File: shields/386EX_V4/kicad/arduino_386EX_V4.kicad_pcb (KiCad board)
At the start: 4 copper layers, 93.3 x 60.3 mm, 50 parts, among them J1 Conn_01x02_Pin, J2 JTAG, J3 Conn_01x04_Pin, J4 Conn_01x04_Pin, J5 Conn_01x04_Pin, J6 SERIAL0, J9 WP Jumper, U1 AT24CS01-STUM, U11 I386EX_PQFP, U2 ULN2003A, U3 SN74LV14A

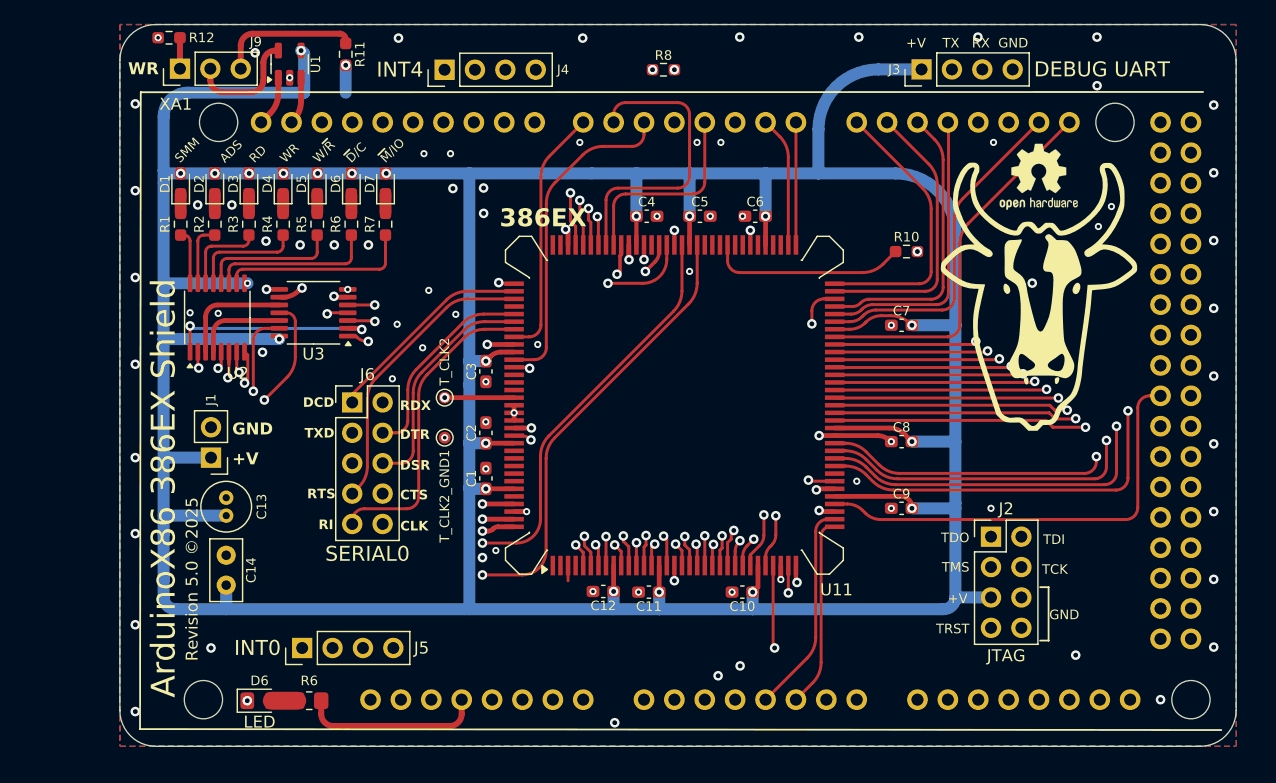
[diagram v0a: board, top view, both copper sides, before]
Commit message: Added I2C SDA, SCK, ~ERROR and ~LOCK pull-up resistors; resolved minor DRC errors.
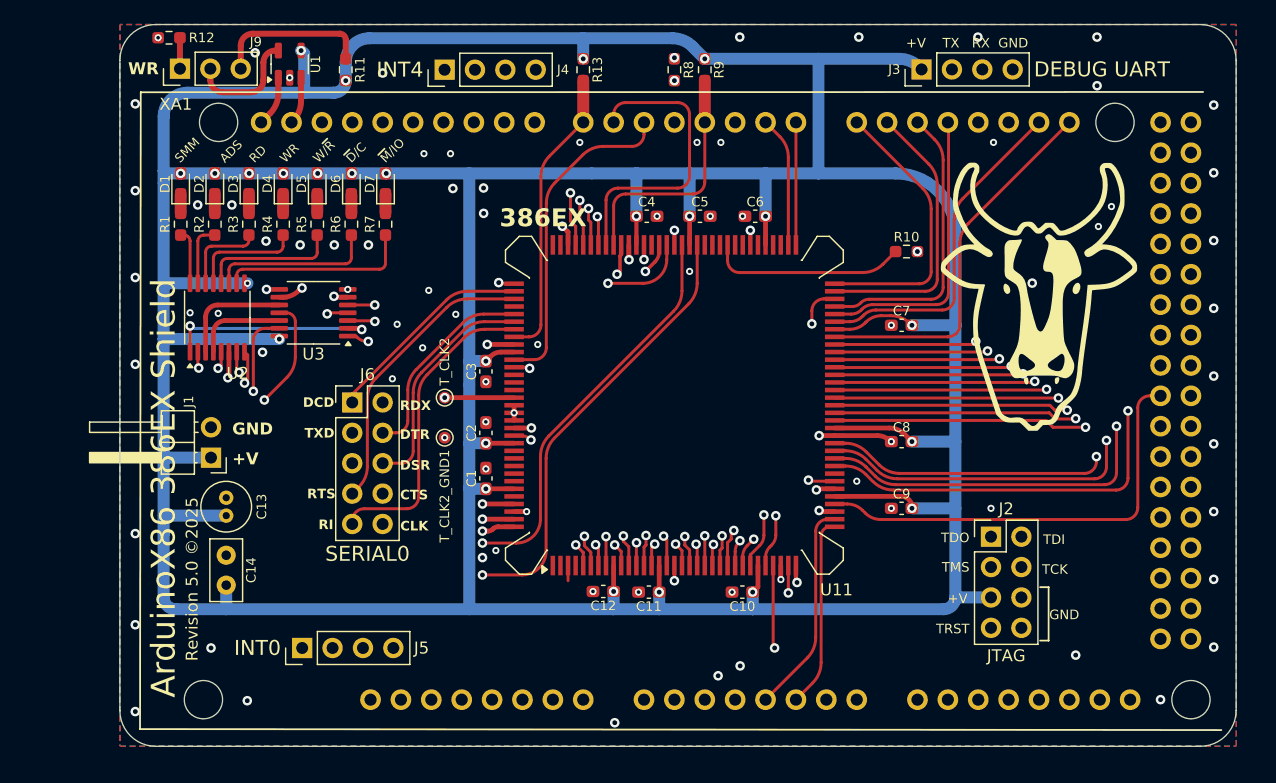
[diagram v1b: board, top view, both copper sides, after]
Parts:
- removed the D6 at (122.2, 120.7)
- removed the R6 at (126.3, 120.7)
- removed REF**: OSHW-Logo2_7.3x6mm_SilkScreen, Symbol:OSHW-Logo2_7.3x6mm_SilkScreen
- added R13: 3.3 K Ohm, Resistor_SMD:R_0603_1608Metric_Pad0.98x0.95mm_HandSolder, F.Cu at (149.2, 67.9)
- added R9: 3.3 K Ohm, Resistor_SMD:R_0603_1608Metric_Pad0.98x0.95mm_HandSolder, F.Cu at (159.4, 67.9)
- C1, C10, C11, C12, C2, C3, C4, C5, C6, C7, C8, C9: value C -> 0.1 uF
- J1: footprint Connector_PinHeader_2.54mm:PinHeader_1x02_P2.54mm_Vertical -> Connector_PinHeader_2.54mm:PinHeader_1x02_P2.54mm_Horizontal
- R11, R12: value R -> 3.3 K Ohm
- moved R11 1.29 mm to (129.4, 67.9)
- moved R8 0.91 mm to (156.8, 67.9), turned to 90 degrees
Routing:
- net +3.3VP: track 380.8 -> 430.4 mm, vias 23 -> 25
- net +3.3V: track 15.1 -> 0.00 mm
- net ~{LOCK}: track 21.1 -> 24.5 mm
- net ~{ERROR}: track 16.9 -> 20.4 mm
- net Net-(U11-CLK2): track 44.0 -> 46.1 mm
- net Net-(D6-A): track 2.13 -> 0.00 mm
- net Net-(J9-Pin_3): track 11.8 -> 13.1 mm
- net /ADS: track 18.1 -> 17.1 mm
- net CLOCK: track 4.40 -> 3.49 mm
- net GND: track 24.0 -> 24.4 mm, vias 86 -> 85

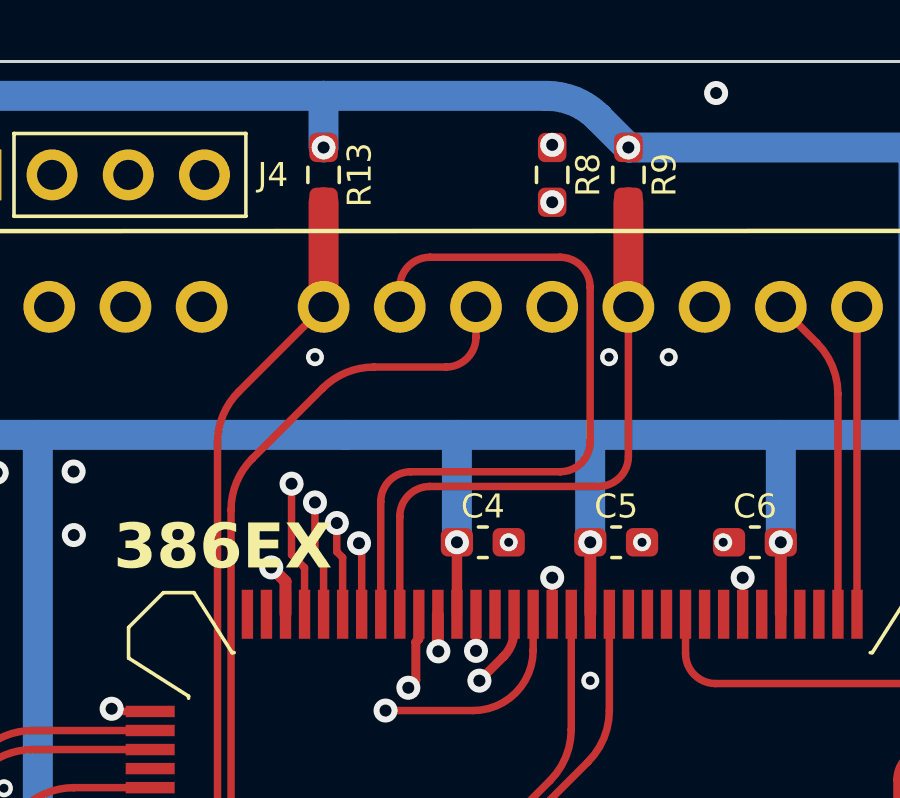
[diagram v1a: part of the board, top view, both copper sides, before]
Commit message: Fixed bug from previous commit, R13 was wired to ~LOCK, was supposed to be to ~BUSY, corrected in this commit.
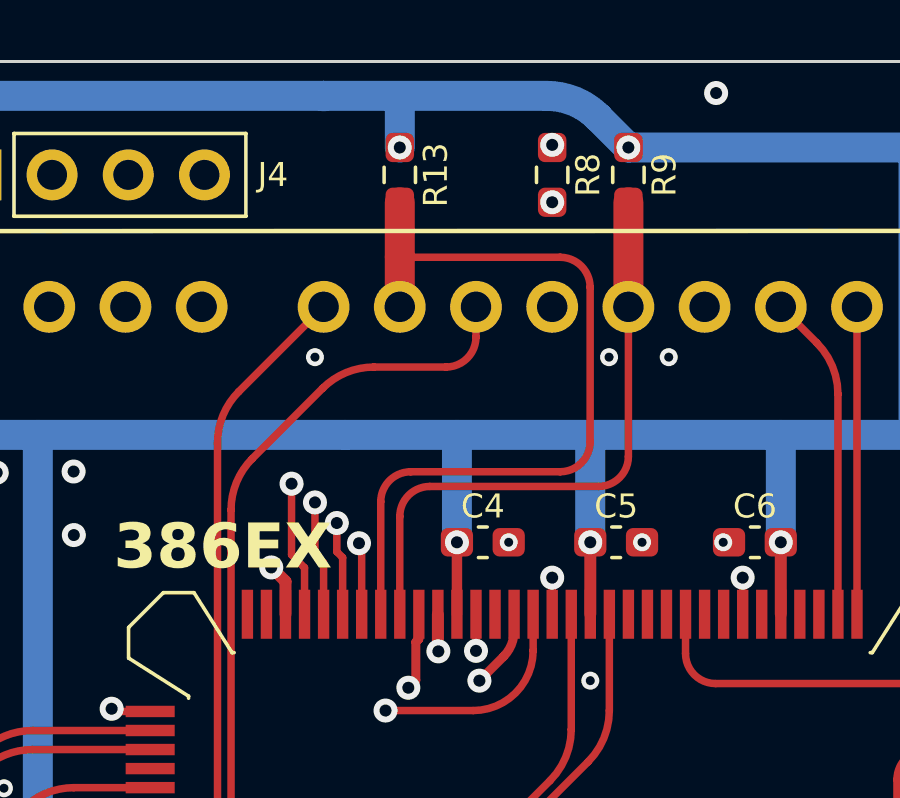
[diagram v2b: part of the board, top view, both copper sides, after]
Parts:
- moved R13 2.54 mm to (151.8, 67.9)
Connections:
- R13 pad 1: ~{LOCK} -> ~{BUSY}
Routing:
- net ~{LOCK}: track 24.5 -> 21.1 mm
- net ~{BUSY}: track 25.0 -> 27.3 mm
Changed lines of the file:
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@@
 	(footprint "Resistor_SMD:R_0603_1608Metric_Pad0.98x0.95mm_HandSolder"
 		(layer "F.Cu")
-		(at 149.225 67.903872 90)
+		(at 151.765 67.903872 90)
 		(descr "Resistor SMD 0603 (1608 Metric), square (rectangular) end terminal, IPC-7351 nominal with elongated pad for handsoldering. (Body size source: IPC-SM-782 page 72, https://www.pcb-3d.com/wordpress/wp-content/uploads/ipc-sm-782a_amendment_1_and_2.pdf), generated with kicad-footprint-generator")
 		(tags "resistor handsolder")
@@
 			(layers "F.Cu" "F.Mask" "F.Paste")
 			(roundrect_rratio 0.25)
-			(net 101 "~{LOCK}")
+			(net 99 "~{BUSY}")
 			(pintype "passive")
 		)
@@
 	)
 	(via
-		(at 149.225 66.991372)
+		(at 151.765 66.991372)
 		(size 0.8)
 		(drill 0.4)
@@
 	)
 	(segment
-		(start 149.225 66.991372)
-		(end 149.225 65.285)
+		(start 151.765 66.991372)
+		(end 151.765 65.285)
 		(width 1)
 		(layer "B.Cu")
@@
 	)
 	(segment
-		(start 157.11 70.65)
-		(end 152.765 70.65)
+		(start 151.13 82.55)
+		(end 151.13 78.8)
 		(width 0.25)
 		(layer "F.Cu")
@@
 	)
 	(segment
-		(start 158.11 71.65)
-		(end 158.11 76.8)
+		(start 157.11 70.65)
+		(end 151.775 70.65)
 		(width 0.25)
 		(layer "F.Cu")
@@
 	)
 	(segment
-		(start 152.13 77.8)
-		(end 157.11 77.8)
-		(width 0.25)
+		(start 151.765 72.3025)
+		(end 151.765 70.64)
+		(width 1)
 		(layer "F.Cu")
 		(net 99)
 	)
 	(segment
-		(start 151.13 78.8)
-		(end 151.13 82.55)
+		(start 158.11 76.8)
+		(end 158.11 71.65)
 		(width 0.25)
 		(layer "F.Cu")
@@
 	)
 	(segment
-		(start 151.765 71.65)
-		(end 151.765 72.3025)
+		(start 151.775 70.65)
+		(end 151.765 70.64)
 		(width 0.25)
 		(layer "F.Cu")
 		(net 99)
 	)
-	(arc
-		(start 158.11 71.65)
-		(mid 157.817106 70.942893)
-		(end 157.11 70.65)
+	(segment
+		(start 151.765 70.64)
+		(end 151.765 68.816372)
+		(width 1)
+		(layer "F.Cu")
+		(net 99)
+	)
+	(segment
+		(start 152.13 77.8)
+		(end 157.11 77.8)
 		(width 0.25)
 		(layer "F.Cu")
@@
 	)
 	(arc
-		(start 152.13 77.8)
+		(start 151.13 78.8)
 		(mid 151.422893 78.092893)
-		(end 151.13 78.8)
+		(end 152.13 77.8)
 		(width 0.25)
 		(layer "F.Cu")
@@
 	)
 	(arc
-		(start 158.11 76.8)
+		(start 157.11 77.8)
 		(mid 157.817106 77.507106)
-		(end 157.11 77.8)
+		(end 158.11 76.8)
 		(width 0.25)
 		(layer "F.Cu")
@@
 	)
 	(arc
-		(start 151.765 71.65)
-		(mid 152.057893 70.942893)
-		(end 152.765 70.65)
+		(start 158.11 71.65)
+		(mid 157.817106 70.942893)
+		(end 157.11 70.65)
 		(width 0.25)
 		(layer "F.Cu")
@@
 		(layer "F.Cu")
 		(net 101)
-	)
-	(segment
-		(start 149.225 72.3025)
-		(end 149.225 68.816372)
-		(width 1)
-		(layer "F.Cu")
-		(net 101)

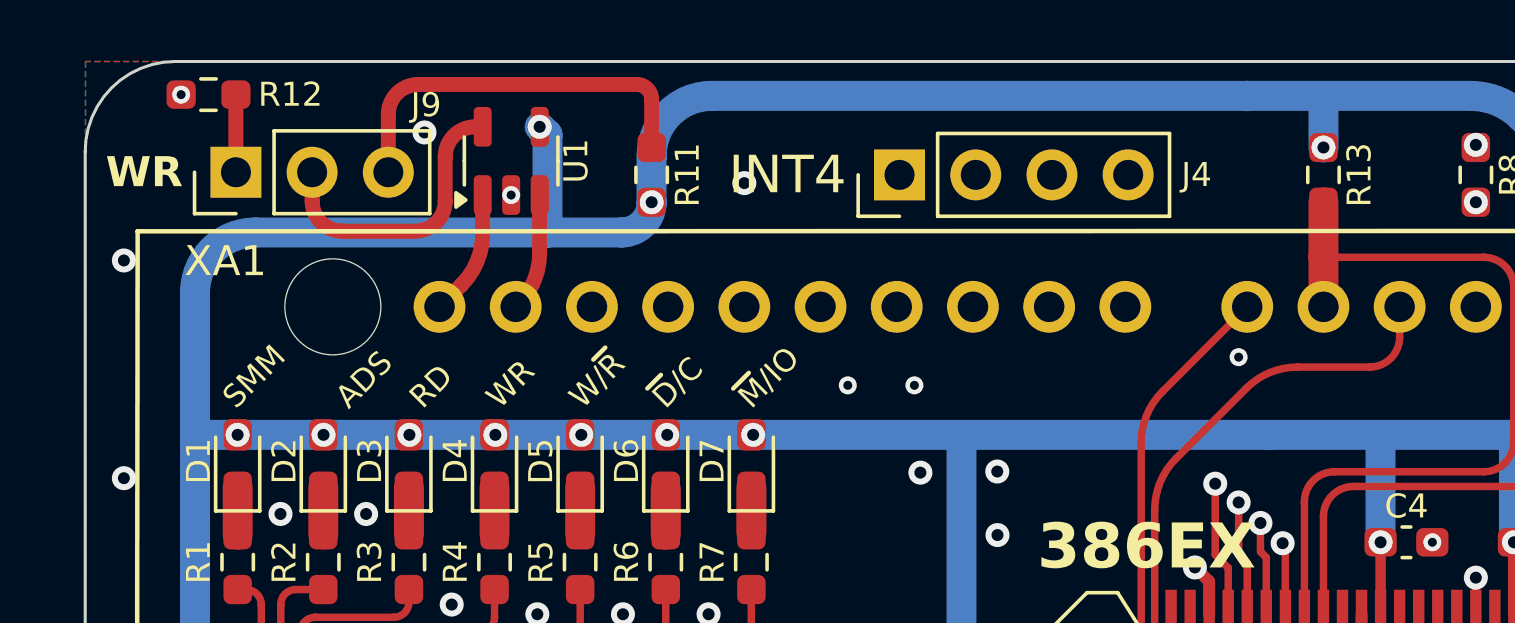
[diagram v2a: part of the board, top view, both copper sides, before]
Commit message: Fixed oversight of I2C SDA and SCK pull-up resistors; rearranged EEPROM IC to accommodate.
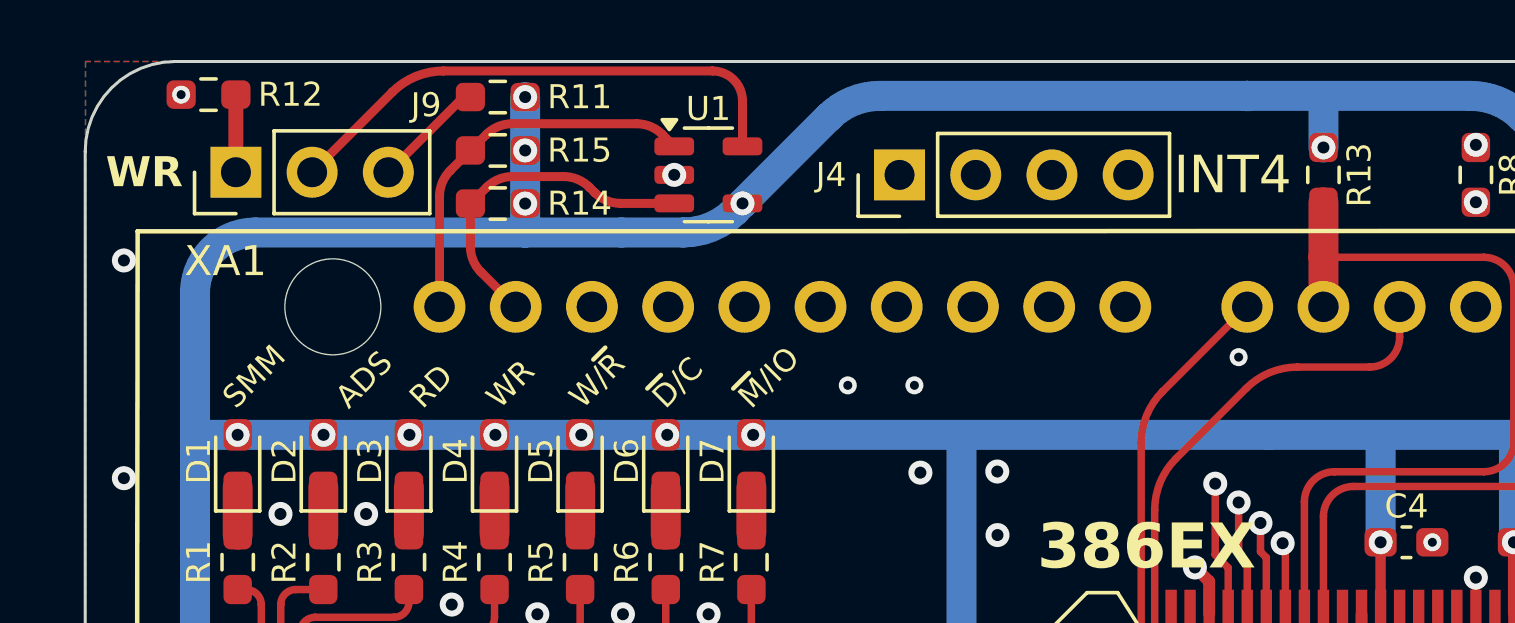
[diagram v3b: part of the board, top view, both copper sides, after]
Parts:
- added R14: 3.3 K Ohm, Resistor_SMD:R_0603_1608Metric_Pad0.98x0.95mm_HandSolder, F.Cu at (124.2, 68.9)
- added R15: 3.3 K Ohm, Resistor_SMD:R_0603_1608Metric_Pad0.98x0.95mm_HandSolder, F.Cu at (124.2, 67.1)
- moved U1 6.59 mm to (131.3, 67.9), turned to 0 degrees
- moved R11 5.75 mm to (124.2, 65.3), turned to 0 degrees
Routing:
- net Net-(J9-Pin_3): track 13.1 -> 3.77 mm
- net SCL: track 4.21 -> 12.9 mm
- net /WP: track 9.72 -> 17.7 mm
- net SDA: track 3.94 -> 11.5 mm
- net +3.3VP: track 430.4 -> 429.8 mm, vias 25 -> 27
- net GND: vias 85 -> 83

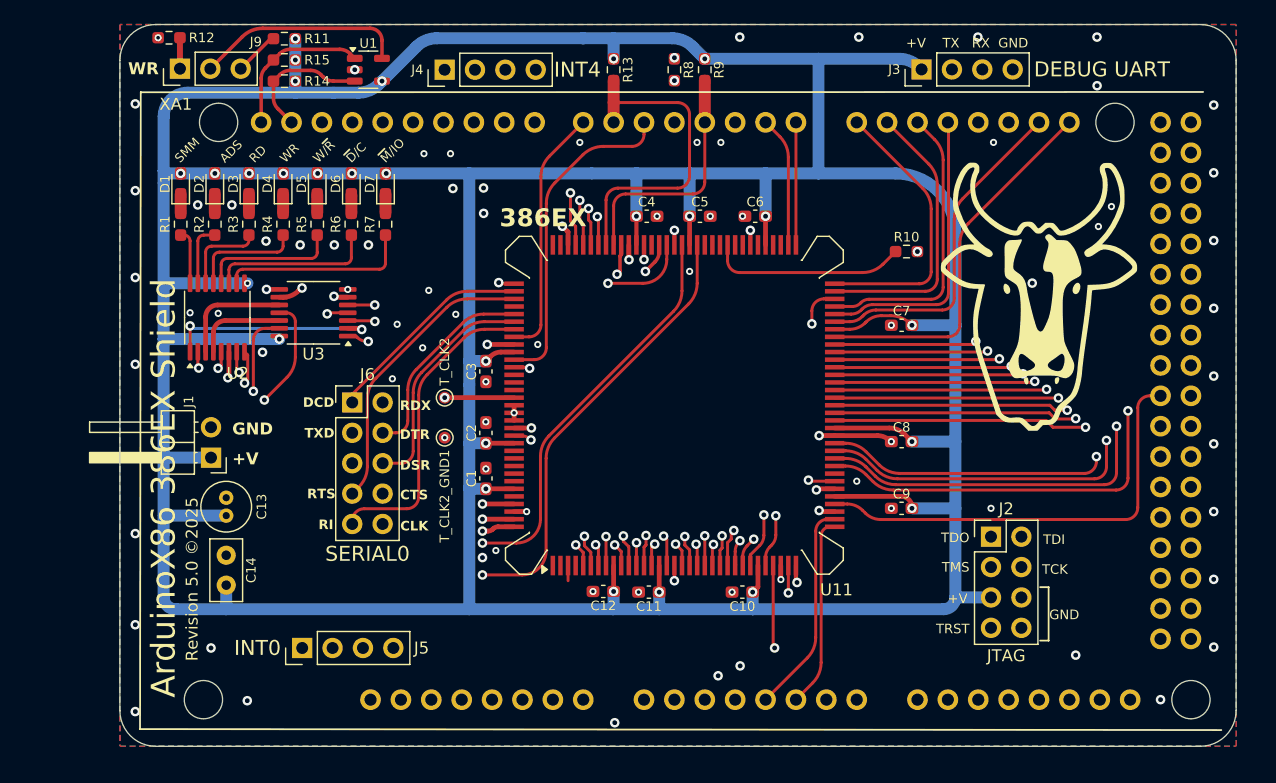
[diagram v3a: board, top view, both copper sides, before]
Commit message: Added 2x 1N4148 diodes for combining 3.3V off-board supplies, updated HTML BOM.
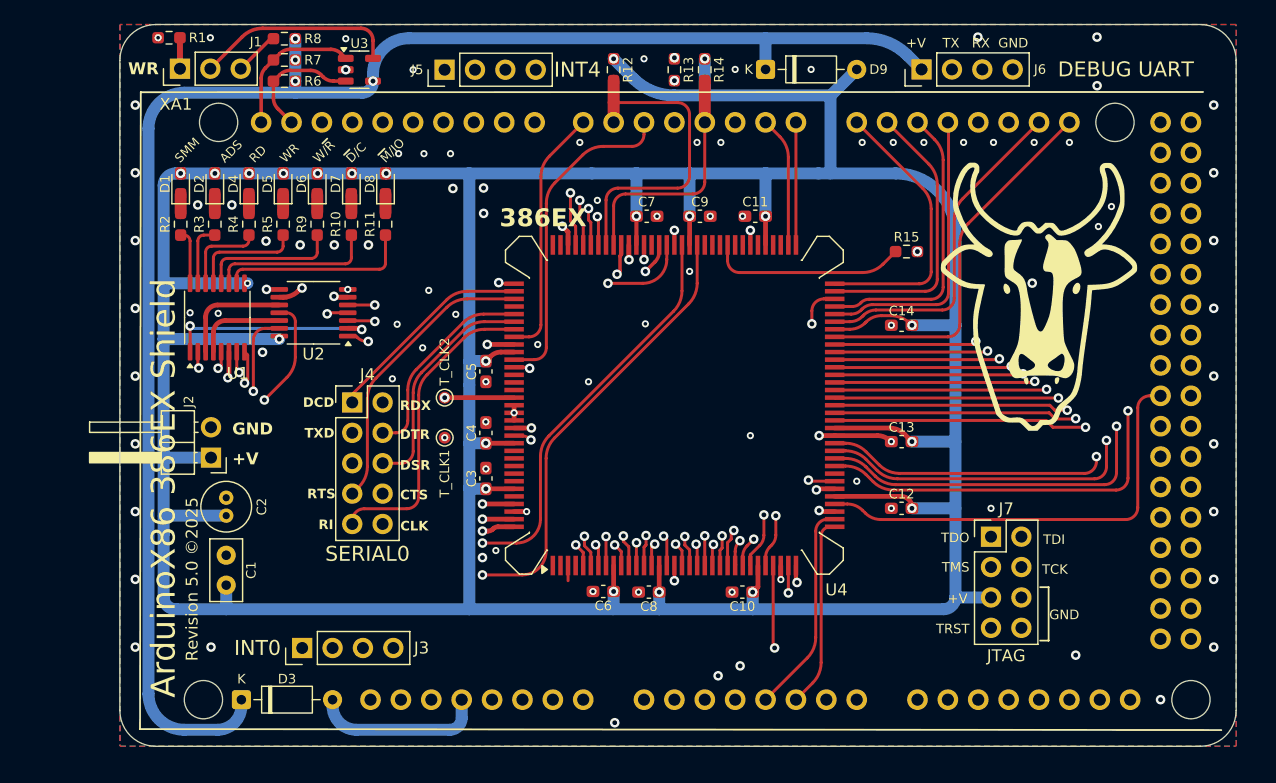
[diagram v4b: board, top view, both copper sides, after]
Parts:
- added D3: 1N4148, Diode_THT:D_DO-35_SOD27_P7.62mm_Horizontal, F.Cu at (120.7, 120.6)
- added D9: 1N4148, Diode_THT:D_DO-35_SOD27_P7.62mm_Horizontal, F.Cu at (164.5, 67.9)
- moved U3 0.75 mm to (130.5, 67.9)
- renumbered C14 to C1, C6 to C11, C9 to C12, C8 to C13, C7 to C14, C13 to C2, C1 to C3, C2 to C4, C3 to C5, C12 to C6, C4 to C7, C11 to C8, C5 to C9, D3 to D4, D4 to D5, D5 to D6, D6 to D7, D7 to D8, J9 to J1, J1 to J2, J5 to J3, J6 to J4, J4 to J5, J3 to J6, J2 to J7, R12 to R1, R6 to R10, R7 to R11, R13 to R12, R8 to R13, R9 to R14, R10 to R15, R1 to R2, R2 to R3, R3 to R4, R4 to R5, R14 to R6, R15 to R7, R11 to R8, R5 to R9, T_CLK2_GND1 to T_CLK1, U2 to U1, U3 to U2, U1 to U3, U11 to U4
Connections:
- J6 pad 1: +3.3VP -> 3.3V_COMBINED
- R6 pad 2: +3.3VP -> 3.3V_COMBINED
- R7 pad 2: +3.3VP -> 3.3V_COMBINED
- R8 pad 2: +3.3VP -> 3.3V_COMBINED
- U3 pad 4: +3.3VP -> 3.3V_COMBINED
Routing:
- net 3.3V_COMBINED: track 0.00 -> 135.1 mm, vias 0 -> 4
- net +3.3VP: track 429.8 -> 373.6 mm, vias 27 -> 23
- net +3.3V: track 0.00 -> 14.4 mm
- net SCL: track 12.9 -> 12.2 mm
- net /WP: track 17.7 -> 16.9 mm
- net SDA: track 11.5 -> 10.8 mm
- net GND: vias 83 -> 98
